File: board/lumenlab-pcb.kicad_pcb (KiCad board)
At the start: 2 copper layers, 100 x 65 mm, 76 parts, among them J1 2.1mm Barrel Jack, J2 01x06, J3 01x04, J4 JTAG, J5 USB_C_Receptacle_USB2.0_16P, SW1 SW_SPST, U1 MP2338, U2 AP7361C-33E, U3 SN74AHCT1G125, U4 SSD1306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

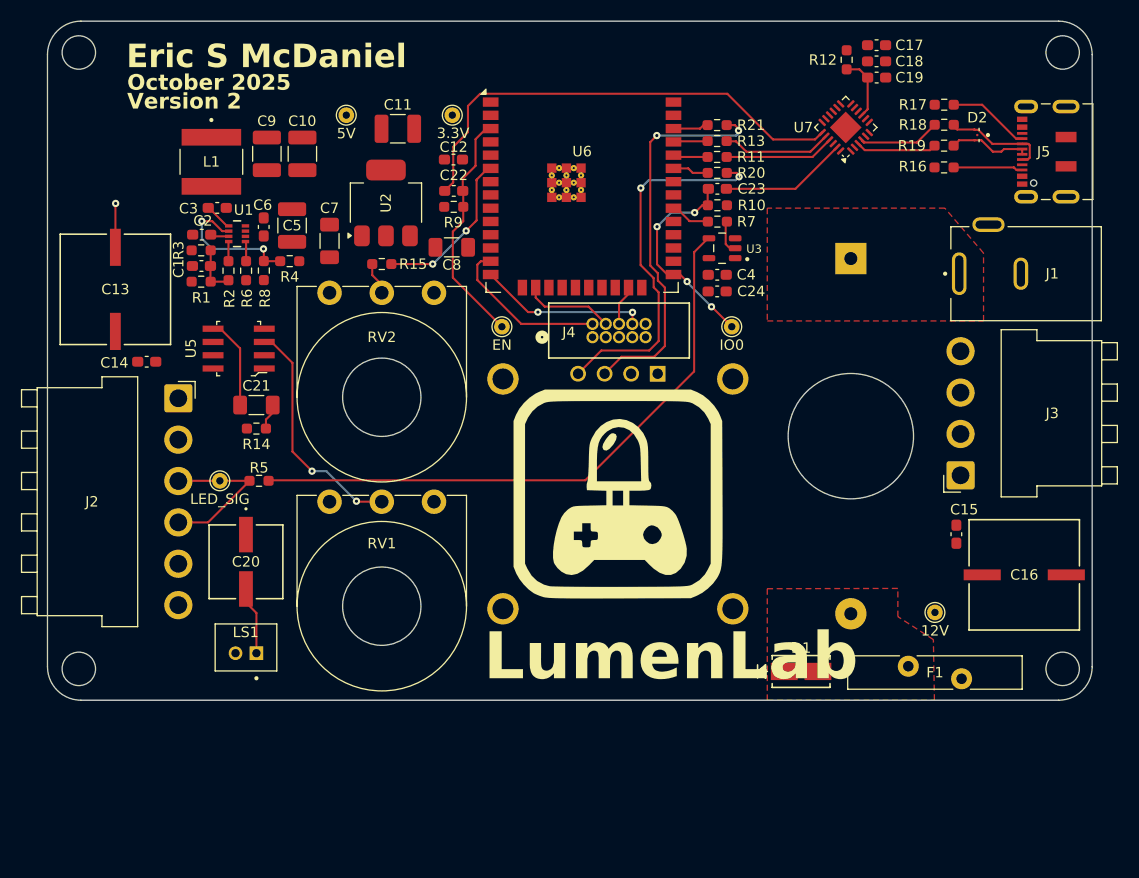
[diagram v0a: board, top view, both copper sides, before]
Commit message: Add 3D preview
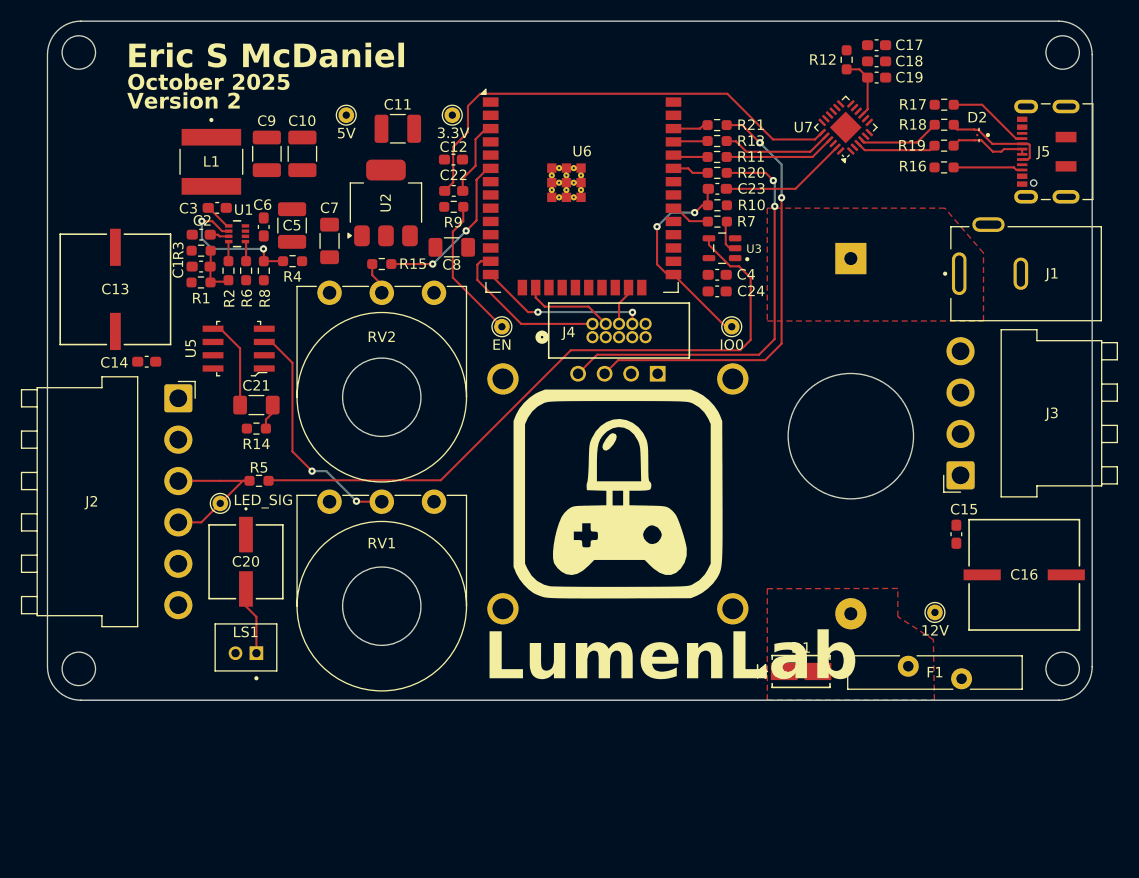
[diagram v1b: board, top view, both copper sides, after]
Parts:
- moved TP6 2.16 mm to (116.5, 116.2)
- moved R4 0.27 mm to (123.5, 93.0)
- moved R1 0.08 mm to (114.7, 95.0)
- moved C1 0.06 mm to (114.7, 93.5)
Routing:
- net Net-(U3-Y): track 58.5 -> 63.6 mm
- net Net-(U4-SCL): track 37.5 -> 42.1 mm
- net Net-(U4-SDA): track 35.6 -> 40.2 mm
- net GND: track 4.21 -> 0.00 mm, vias 1 -> 0
- net /ESP32_EN: track 22.9 -> 21.3 mm
- net /ESP32_GPIO0: track 20.9 -> 21.5 mm, vias 4 -> 2

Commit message: Promote to four-layer board
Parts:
- TP1, TP2, TP3, TP4, TP5, TP6: footprint TestPoint:TestPoint_THTPad_D1.5mm_Drill0.7mm -> TestPoint:TestPoint_THTPad_D2.0mm_Drill1.0mm
- moved C15 2.67 mm to (187.9, 116.6), turned to 0 degrees
- moved J1 1.04 mm to (194.2, 94.2)
- moved J5 0.47 mm to (196.8, 82.5)
- moved J3 0.30 mm to (187.1, 113.4)
- moved J2 0.22 mm to (112.7, 106.1)
- moved TP6 0.15 mm to (116.7, 116.2)
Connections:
- J4 pad 1: +3.3V -> +5V
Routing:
- net Net-(U3-Y): track 63.6 -> 0.00 mm
- net Net-(U7-~{RTS}): track 45.8 -> 0.00 mm
- net Net-(U4-SCL): track 42.1 -> 0.00 mm, vias 2 -> 0
- net Net-(U4-SDA): track 40.2 -> 0.00 mm, vias 2 -> 0
- net /AMP_IN: track 22.6 -> 0.00 mm, vias 2 -> 0
- net /ESP32_EN: track 21.3 -> 0.04 mm
- net /ESP32_GPIO0: track 21.5 -> 0.42 mm, vias 2 -> 0
- net /ESP32_GPIO12: track 16.2 -> 0.00 mm, vias 2 -> 0
- net /ESP32_GPIO14: track 15.6 -> 0.00 mm
- net /ESP32_GPIO34: track 15.6 -> 0.00 mm, vias 2 -> 0
- net /LED_DIN: track 15.3 -> 0.00 mm
- net /BUCK_EN: track 13.7 -> 0.00 mm, vias 2 -> 0
- net Net-(U7-~{DTR}): track 12.2 -> 0.00 mm
- net Net-(C20-Pad1): track 8.79 -> 0.00 mm
- net /ESP32_GPIO13: track 8.71 -> 0.00 mm
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- removed copper zone on F.Cu, net /FUSE
- removed copper zone on F.Cu, net Net-(SW1-A)
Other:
- copper layers 2 -> 4
- board text added: "October 2025 · Version 2"
- board text removed: "October 2025"
- board text removed: "Version 2"

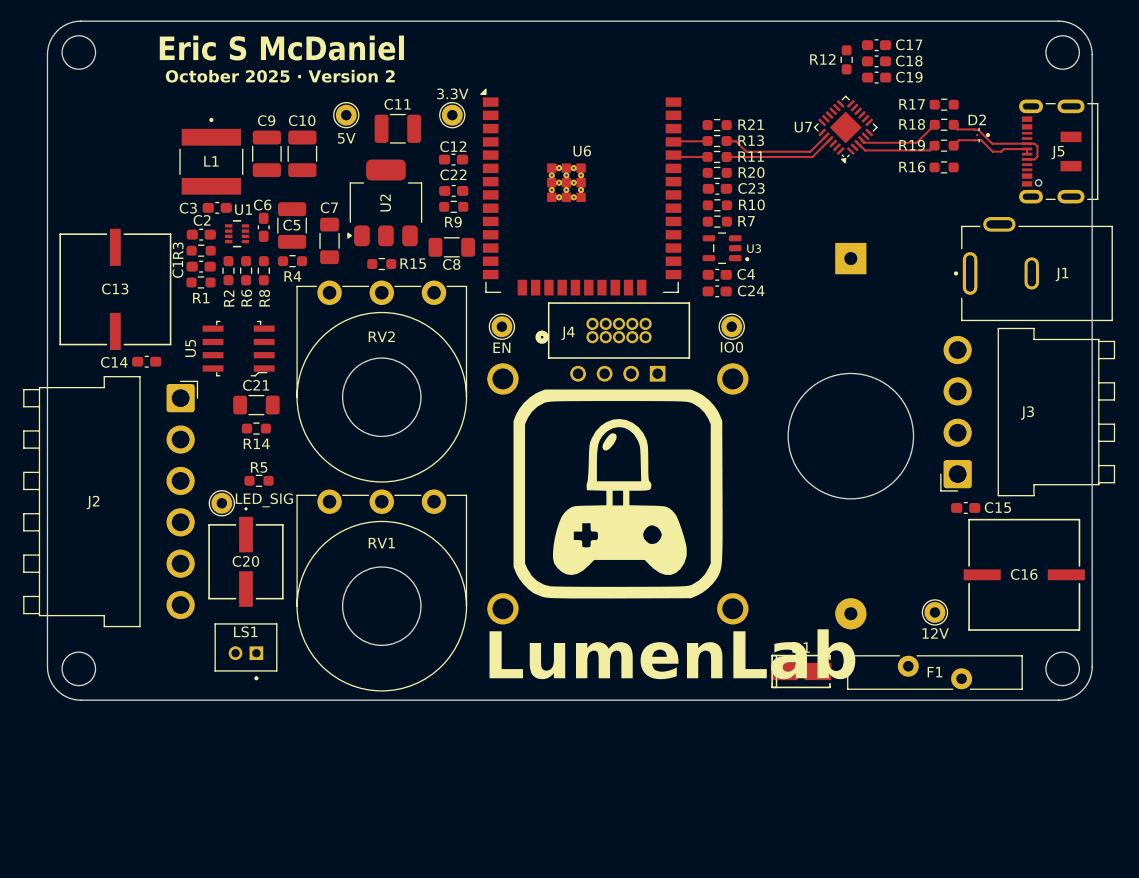
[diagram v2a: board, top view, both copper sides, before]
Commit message: Setup for trace routing, DRC fixes
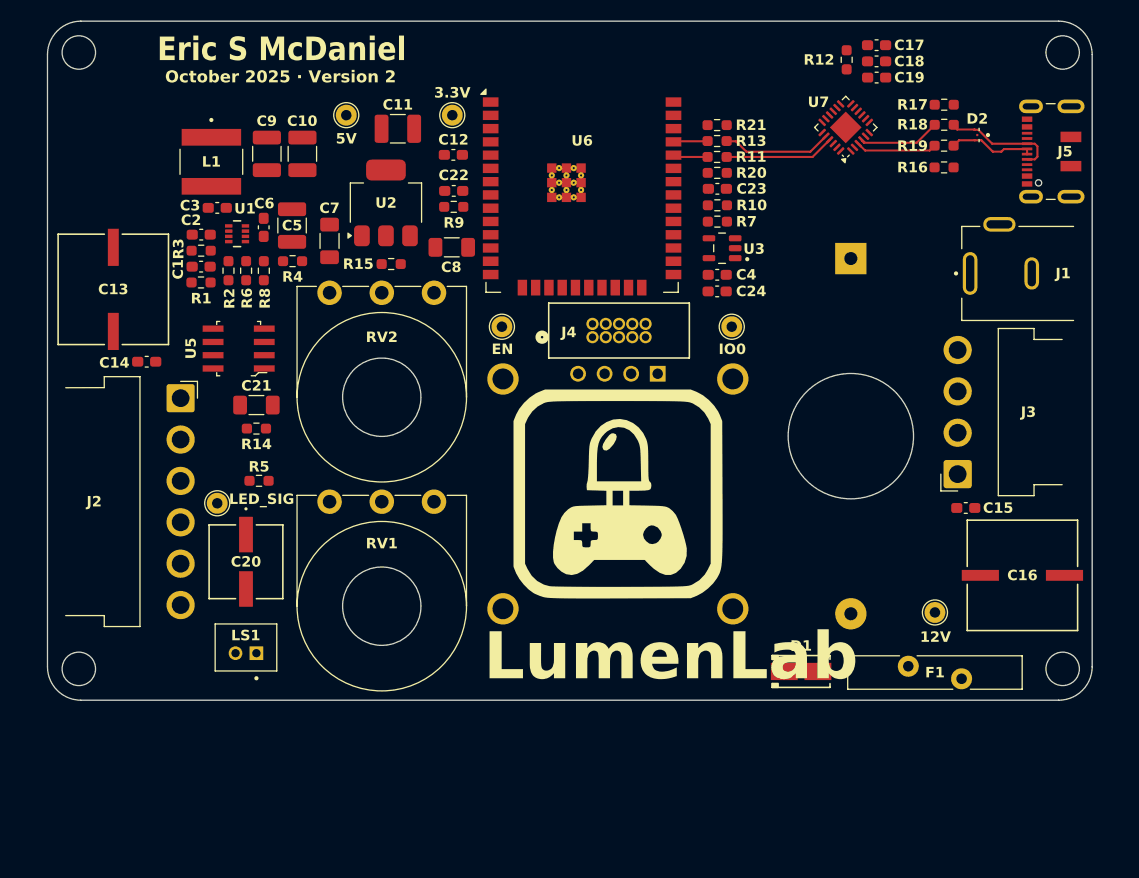
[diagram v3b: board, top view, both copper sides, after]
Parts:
- J2: footprint Connector_JST:JST_VH_B6PS-VH_1x06_P3.96mm_Horizontal -> 2_Custom_SilkscreenTrimmed:JST_VH_1x06_P3.96_SilkscreenTrimmed
- J3: footprint Connector_JST:JST_VH_B4PS-VH_1x04_P3.96mm_Horizontal -> 2_Custom_SilkscreenTrimmed:JST_VH_1x04_P3.96mm_SilkscreenTrimmed
- J5: footprint Connector_USB:USB_C_Receptacle_JAE_DX07S016JA1R1500 -> 2_Custom_SilkscreenTrimmed:USB_C_Receptacle_JAE_DX07S016JA1R1500
- U6: value ESP32-WROOM-32E -> 2_Vendor_ESP32_WROOM_32E; footprint RF_Module:ESP32-WROOM-32E -> ESP32-WROOM-32E:2_Vendor_ESP32_WROOM_32E
- moved R15 0.90 mm to (132.9, 93.2)
- moved C12 0.45 mm to (138.8, 82.8)
- moved TP6 0.44 mm to (116.2, 116.2)
- moved C13 0.20 mm to (106.3, 95.7)
- moved C16 0.18 mm to (193.3, 123.0)
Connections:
- J5 pad A4: unconnected-(J5-VBUS-PadA4) -> (no net)
- J5 pad A9: unconnected-(J5-VBUS-PadA4)_1 -> (no net)

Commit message: Replace toggle switch with rocker switch because board real estate is expensive
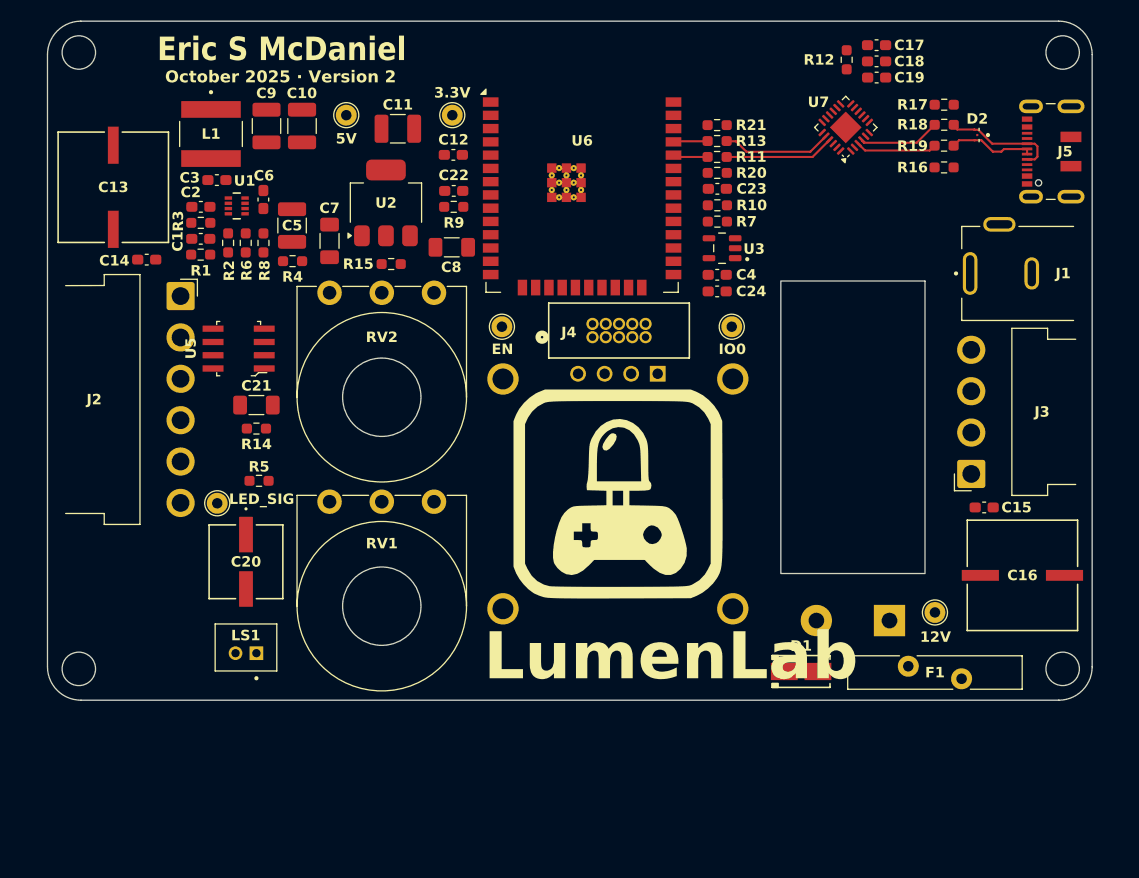
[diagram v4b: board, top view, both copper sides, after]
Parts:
- SW1: footprint 2_Custom_PowerSwitch:PowerSwitch -> 2_Custom_PowerSwitch:RockerPowerSwitch
- moved J2 9.77 mm to (112.7, 96.3)
- moved C13 9.77 mm to (106.3, 85.9)
- moved C14 9.77 mm to (109.5, 92.8)
- moved C10 2.66 mm to (124.4, 80.0)
- moved C9 2.66 mm to (121.0, 80.0)
- moved L1 2.66 mm to (115.7, 80.8)
- moved R1 2.66 mm to (114.7, 92.3)
- moved R2 2.66 mm to (117.3, 91.2)
- moved R6 2.66 mm to (119.0, 91.2)
- moved U1 2.66 mm to (118.1, 87.7)
- moved C1 2.66 mm to (114.7, 90.8)
- moved C2 2.66 mm to (114.7, 87.8)
- moved C3 2.66 mm to (116.2, 85.2)
- moved C6 2.66 mm to (120.7, 87.1)
- moved R3 2.66 mm to (114.7, 89.3)
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
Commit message: Complete redesign of board to include 8Ω speaker
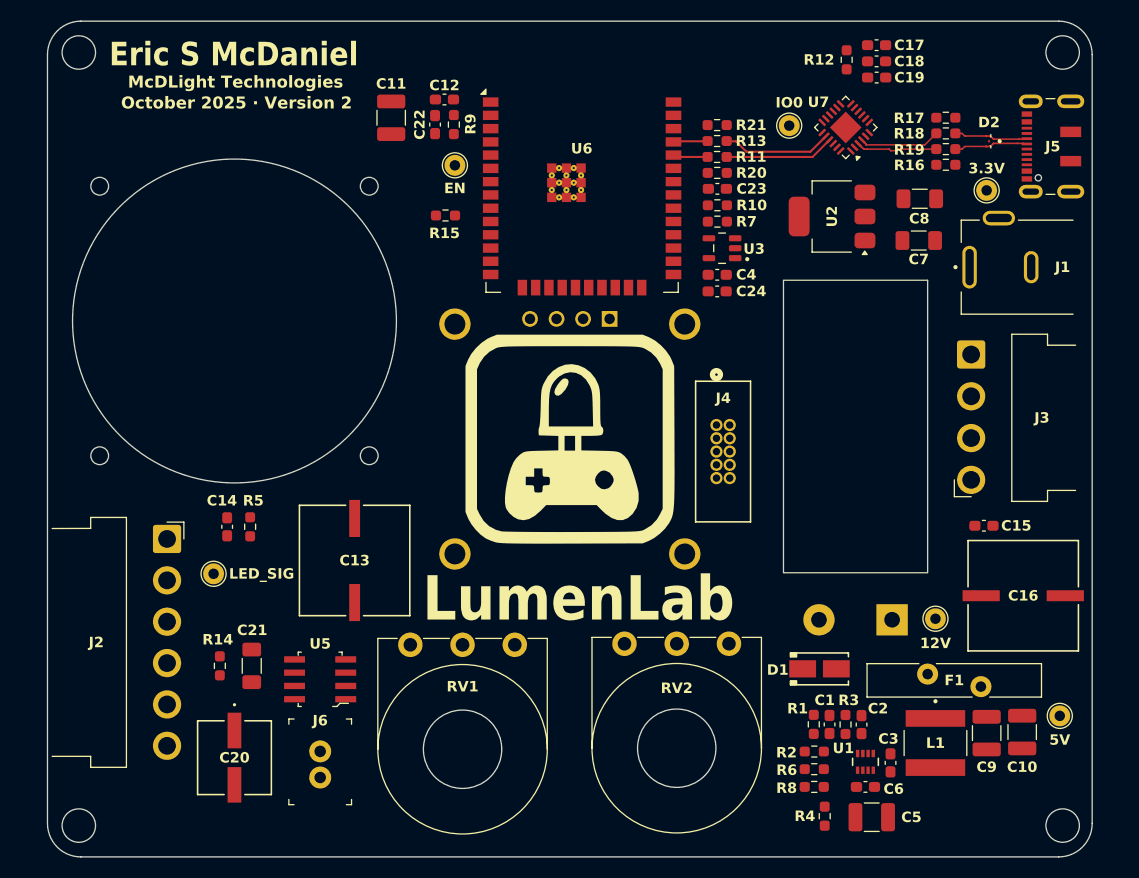
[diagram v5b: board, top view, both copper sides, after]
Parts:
- added J6: B2B-XH-A_LF__SN_, digikey-footprints:PinHeader_1x2_P2.5mm_Drill1.1mm, F.Cu at (126.1, 142.4)
- LS1: footprint 2_Custom_JST-AudioSpeaker:JST_B2B-PH-K-S -> 2_Custom_JST-AudioSpeaker:Speaker; moved to B.Cu
- U6: footprint ESP32-WROOM-32E:2_Vendor_ESP32_WROOM_32E -> 2_Vendor_ESP32_WROOM_32E:ESP32_WROOM_32E
- moved L1 90.6 mm to (185.0, 139.1)
- moved C9 90.2 mm to (189.9, 138.2)
- moved C10 90.1 mm to (193.3, 138.1)
- moved TP5 89.3 mm to (196.9, 136.5)
- moved C3 85.3 mm to (180.7, 141.0), turned to -90 degrees
- moved C6 80.5 mm to (178.3, 143.3), turned to 0 degrees
- moved C2 80.3 mm to (177.9, 137.3), turned to -90 degrees
- moved U1 80.3 mm to (178.3, 140.9), turned to 90 degrees
- moved C5 79.3 mm to (178.9, 146.2), turned to 0 degrees
- moved R3 78.2 mm to (176.4, 137.3), turned to 90 degrees
- moved C1 76.1 mm to (174.9, 137.3), turned to 90 degrees
- moved R2 74.3 mm to (173.4, 139.9), turned to 180 degrees
- moved R6 74.2 mm to (173.4, 141.6), turned to 180 degrees
- moved R8 74.1 mm to (173.4, 143.3), turned to 180 degrees
- moved R1 73.9 mm to (173.3, 137.3), turned to 90 degrees
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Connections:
- J5 pad A4: (no net) -> unconnected-(J5-VBUS-PadA4)
- J5 pad A9: (no net) -> unconnected-(J5-VBUS-PadA4)_1
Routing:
- net /USB_D-: track 11.0 -> 7.12 mm
- net /USB_D+: track 8.34 -> 7.11 mm
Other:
- board size 100 x 65 mm -> 100 x 80 mm
- board text added: "12V"
- board text added: "3.3V"
- board text added: "5V"
- board text added: "EN"
- board text added: "IO0"
- board text added: "LED_SIG"
- board text added: "McDLight Technologies"

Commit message: YARD (yet another redesign) - Keep light current paths short and together
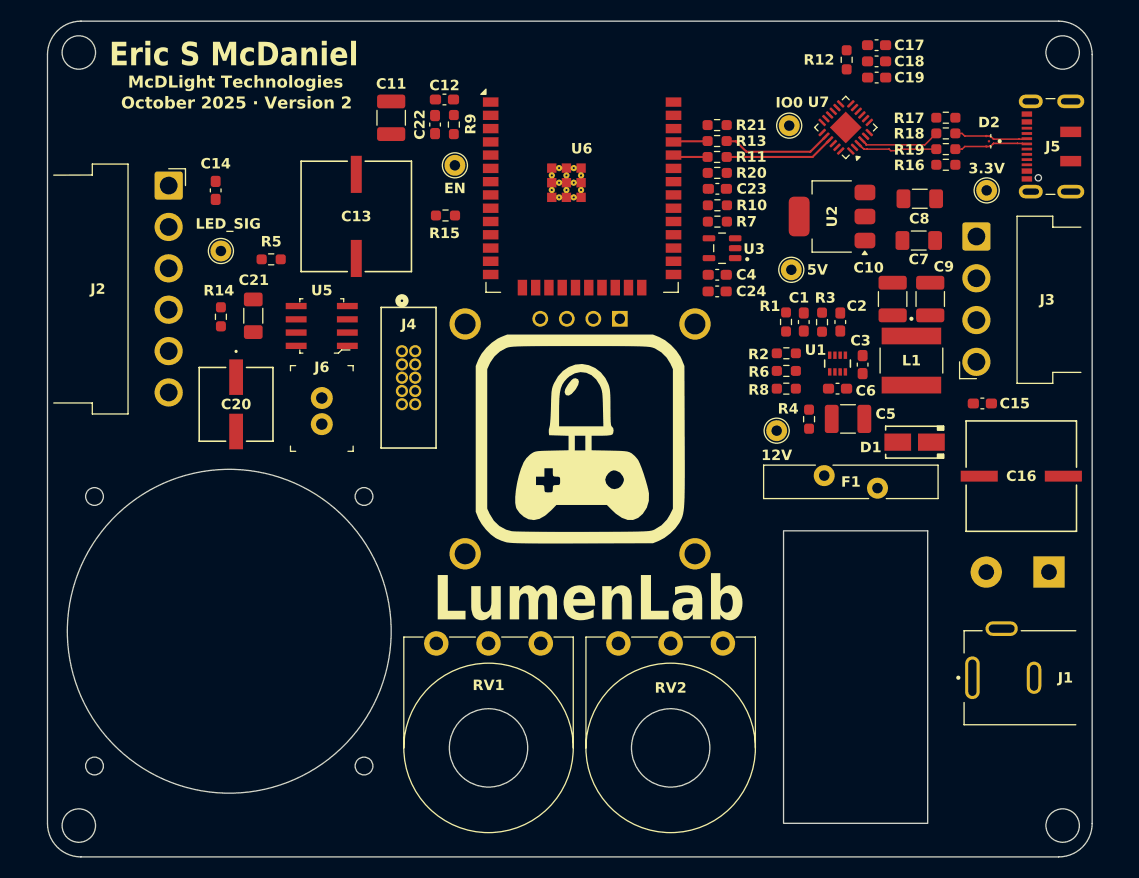
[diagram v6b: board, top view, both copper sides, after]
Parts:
- moved TP5 49.8 mm to (171.2, 93.8)
- moved C10 43.3 mm to (180.9, 96.6), turned to 90 degrees
- moved C9 41.9 mm to (184.5, 96.6), turned to 90 degrees
- moved J1 39.3 mm to (194.4, 132.8)
- moved R1 38.6 mm to (170.7, 98.8)
- moved C1 38.6 mm to (172.4, 98.8)
- moved C2 38.6 mm to (175.9, 98.8)
- moved R3 38.6 mm to (174.1, 98.8)
- moved C6 38.2 mm to (175.6, 105.2)
- moved R8 38.2 mm to (170.7, 105.2)
- moved C3 38.2 mm to (178.0, 102.9)
- moved U1 38.2 mm to (175.6, 102.8)
- moved R2 38.2 mm to (170.7, 101.8)
- moved R6 38.2 mm to (170.7, 103.5)
- moved C5 38.2 mm to (176.6, 108.1)
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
